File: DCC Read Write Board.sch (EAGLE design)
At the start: 159 parts, among them IC5 4163D, J103 686318124422, J111 PTR1PAD1-17, J112 PTR1PAD1-17, J121 PTR1PAD1-17, J122 PTR1PAD1-17, K1 68613014122, Q1 MUN2211T1, Q101 TDA1317, Q102 2SC2712GR, Q103 2SC2712GR, Q104 2SD99CL, Q106 2SC2712GR, Q151 TDA1316, Q180 2SC2712GR, Q181 744053D, Q182 74HCT175D, Q183 74HC00D, Q190 2SC2712GR, Q2 BCX71SMD, U185 74HC02D

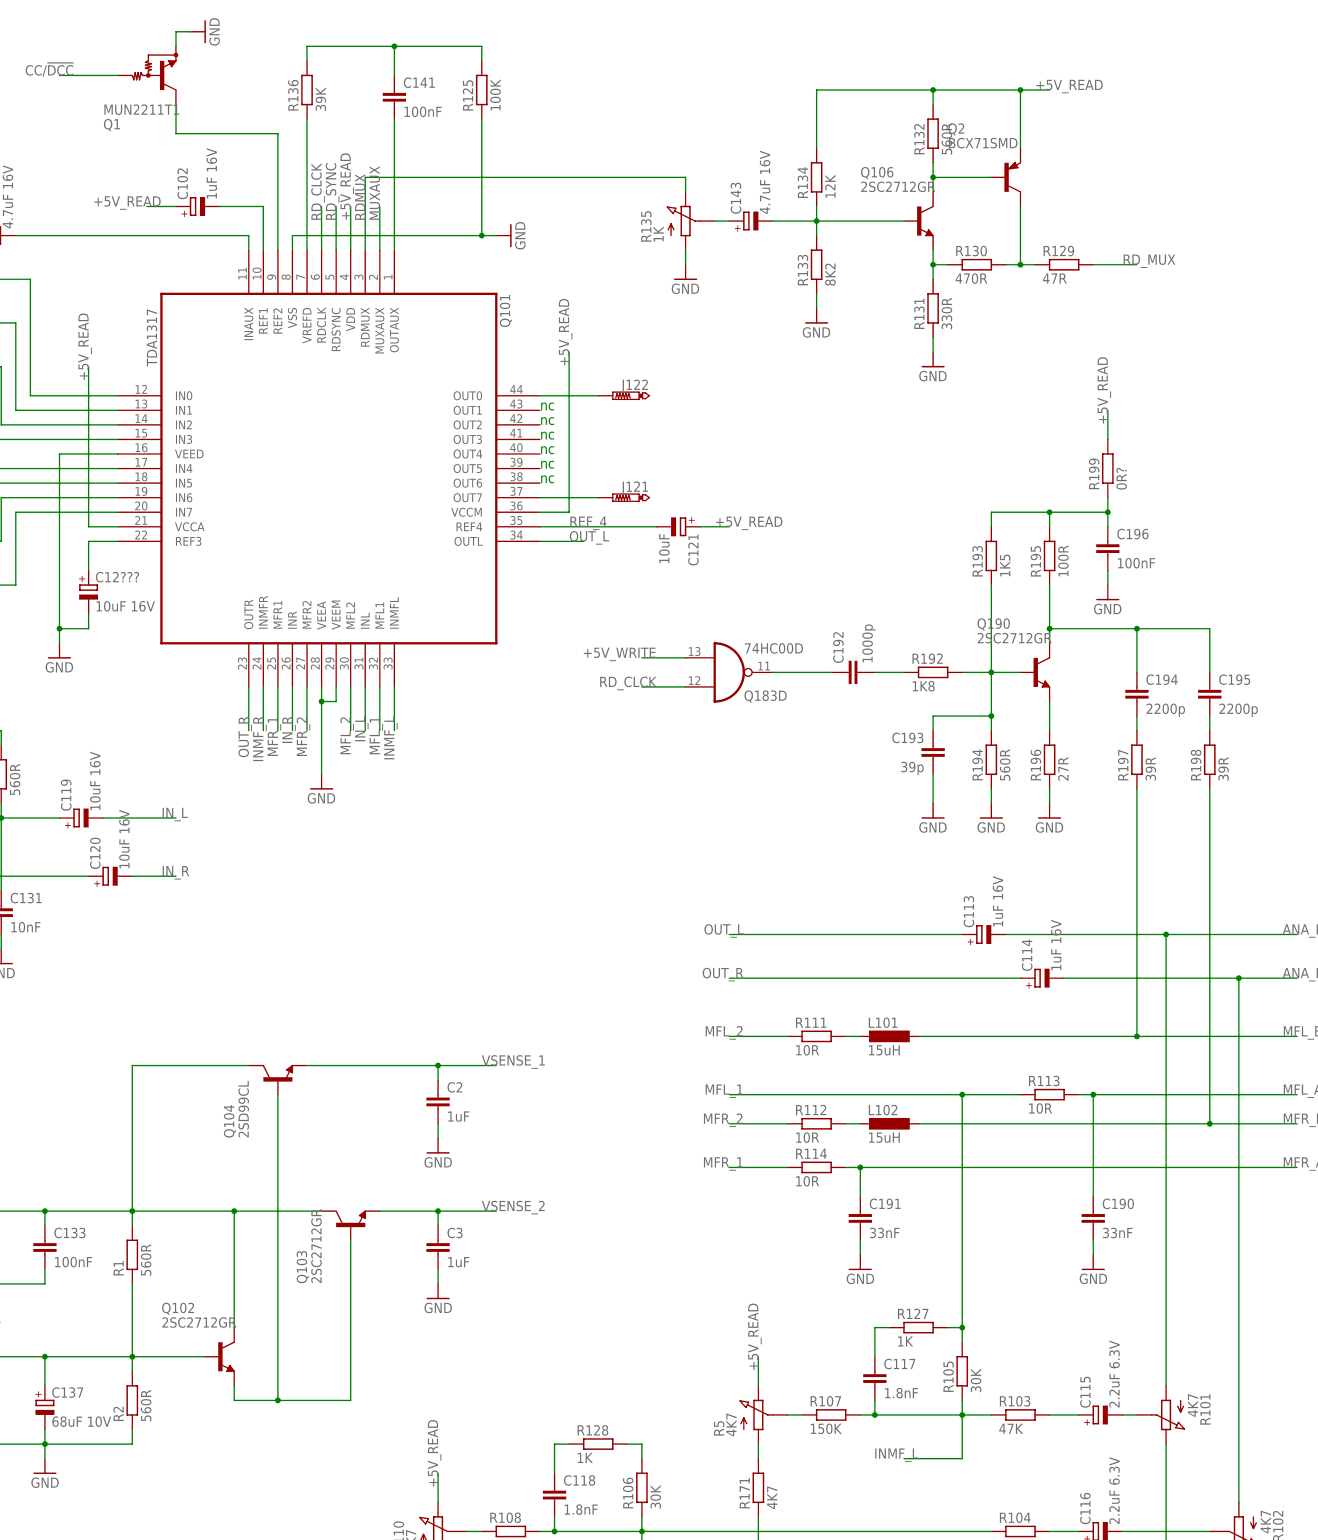
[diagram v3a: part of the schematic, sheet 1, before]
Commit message: Started placing more passives
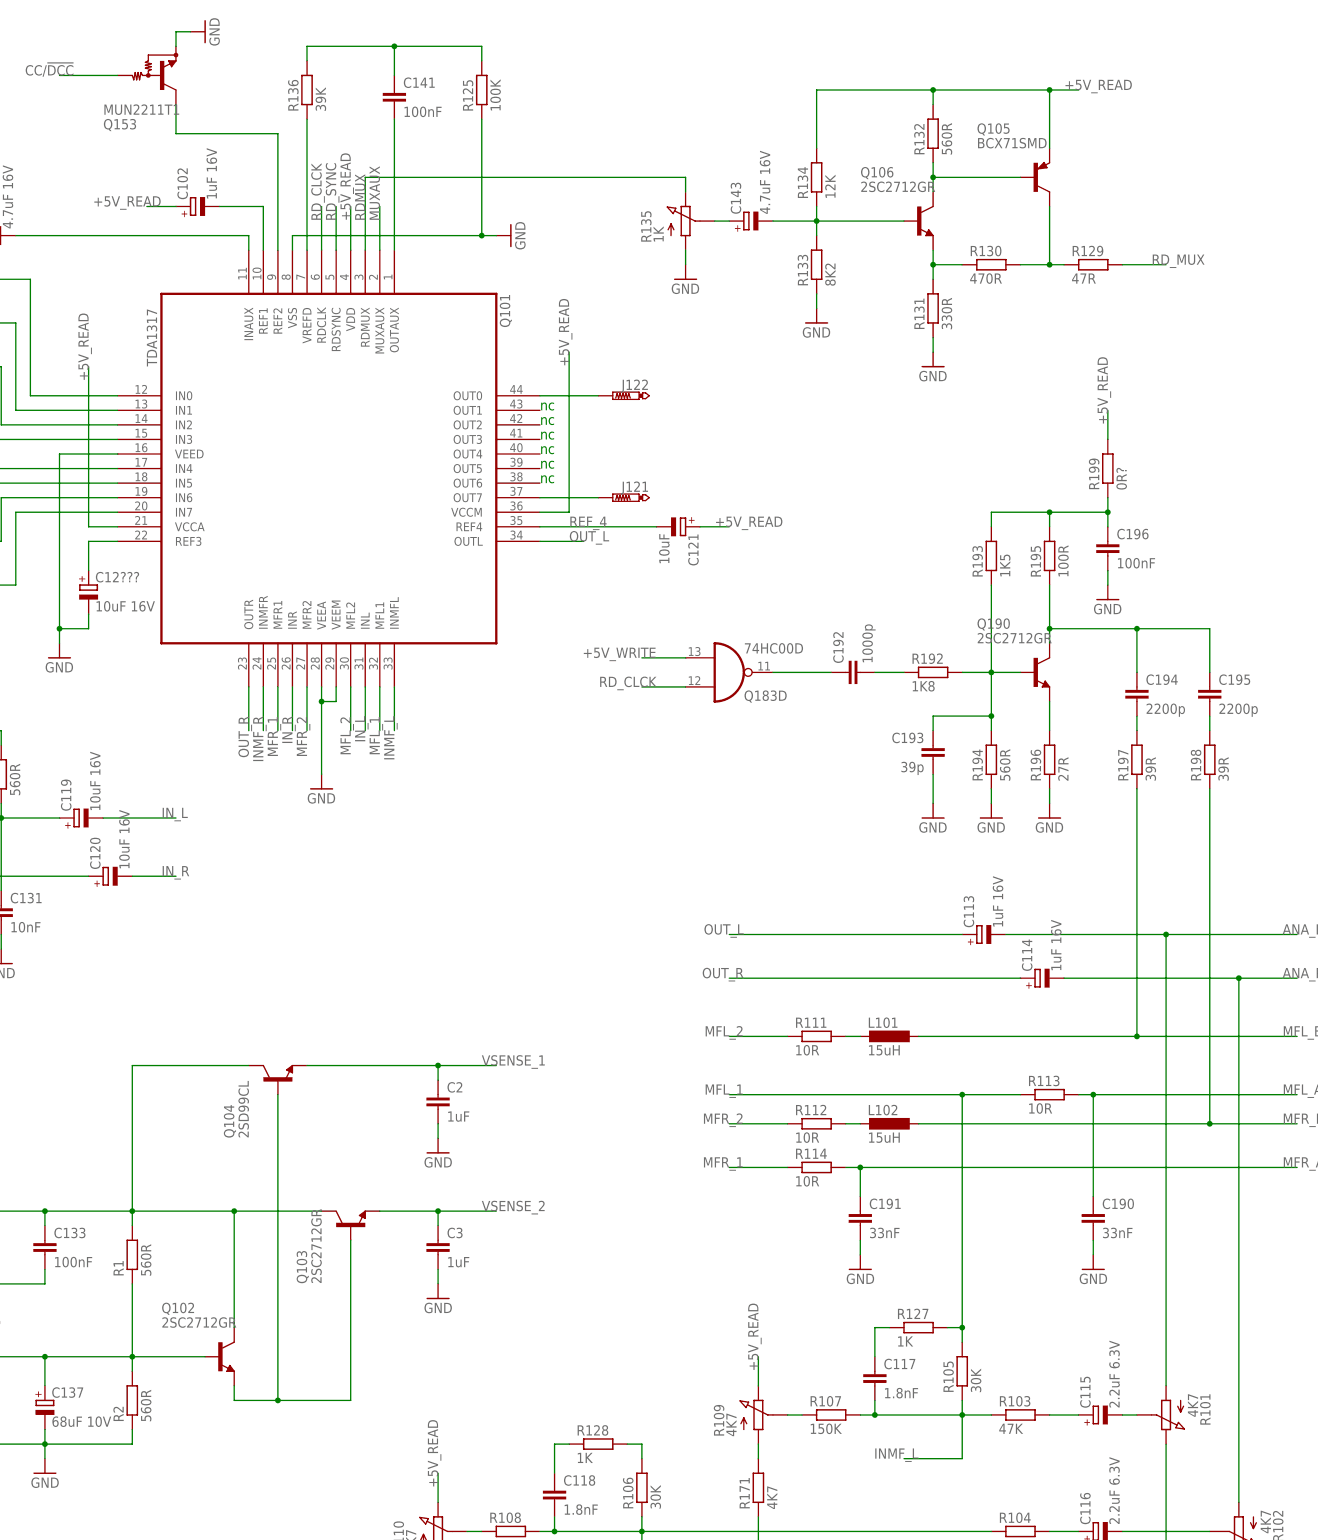
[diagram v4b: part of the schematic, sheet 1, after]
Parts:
- removed Q2: BCX71SMD, transistor-pnp:BCX71SMD
- added Q105: BCX71SMD, transistor-pnp:BCX71SMD
- C115, C116: device rcl:CPOL-EU153CLV-0505 -> rcl:CPOL-EUC/6032-28R
- C135, C137, C150: device rcl:CPOL-EU153CLV-0405 -> rcl:CPOL-EUE
- renumbered Q1 to Q153, R5 to R109
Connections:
- net +5V_READ: now also Q105.E; no longer Q2.E
- net N$83: now also Q105.B; no longer Q2.B
- net N$84: now also Q105.C; no longer Q2.C
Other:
- moved on the sheet: R129, R130

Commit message: Initial parts placement done
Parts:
- removed R1, R2: 560R, rcl:R-EU_R0603
- added R121: 6K8, rcl:R-EU_R0603
- added R122: 68K, rcl:R-EU_R0603
- C102, C113, C114: device rcl:CPOL-EU153CLV-0505 -> rcl:CPOL-EUB/3528-21W
- C148: device rcl:CPOL-EU153CLV-0405 -> rcl:CPOL-EUE
- J111, J112, J121, J122: value PTR1PAD1-17 -> PTR1TP18SQ; device testpad:PTR1PAD1-17 -> testpad:PTR1TP18SQ
- R187: device ptc-ntc:NTC640 -> ptc-ntc:B57164
- renumbered C1 to C184, C2 to C144, C3 to C145, C4 to C182, IC5 to Q184, K1 to J101, R3 to R116, R4 to R115
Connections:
- net +8V: now also R121.2; no longer R1.2
- net GND: now also R122.1; no longer R2.1
- net MFL_A: now also J101.5
- net MFL_B: now also J101.2
- net MFR_A: now also J101.8
- net MFR_B: now also J101.6
- net N$52: now also R121.1, R122.2; no longer R1.1, R2.2
